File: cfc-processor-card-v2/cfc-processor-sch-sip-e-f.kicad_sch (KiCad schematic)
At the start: 5 parts, among them U7 OSD3358-1G-ISM

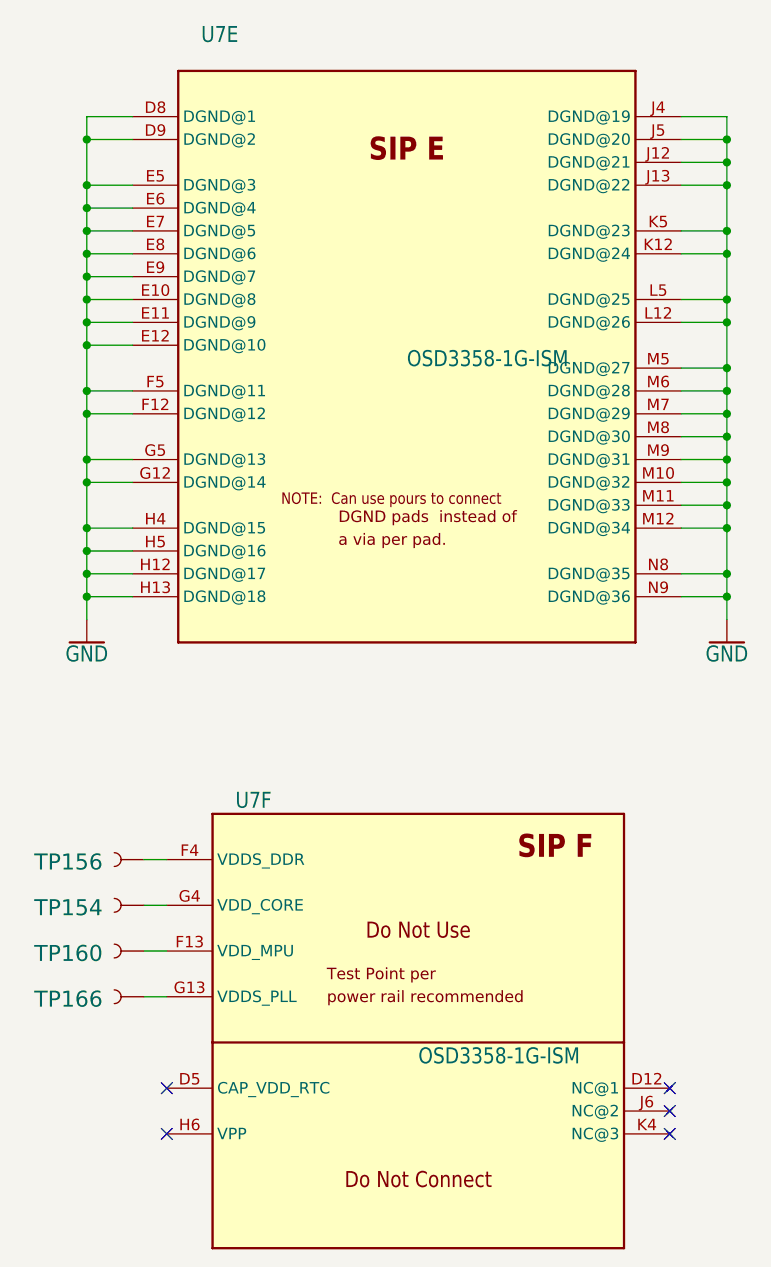
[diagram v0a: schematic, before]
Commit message: CFC processor schematic Change
changed to hierarchy view, changed all global net labels to hierarchy labels, changed all resistor, capacitor, and ground symbols to modern oresat labels. Deleted connectors sheet and added .history to gitignore.
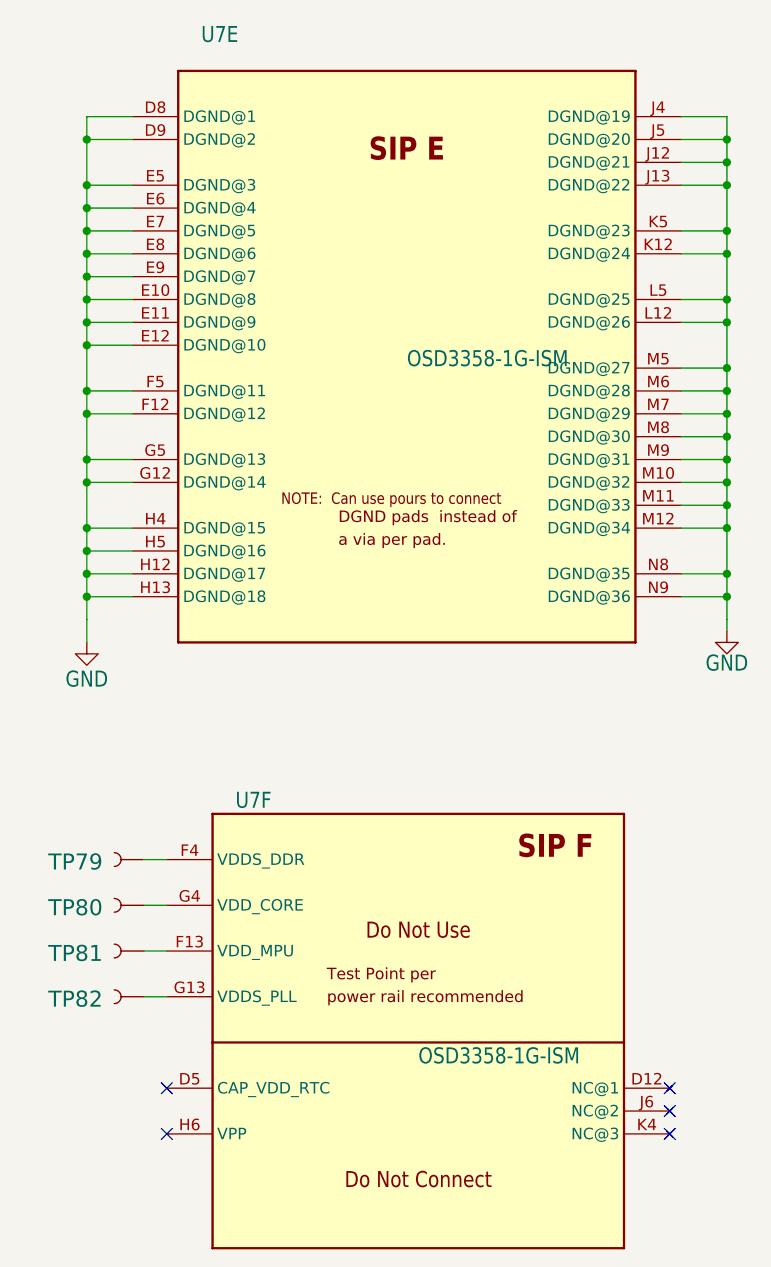
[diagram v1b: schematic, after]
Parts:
- renumbered TP156 to TP79, TP154 to TP80, TP160 to TP81, TP166 to TP82

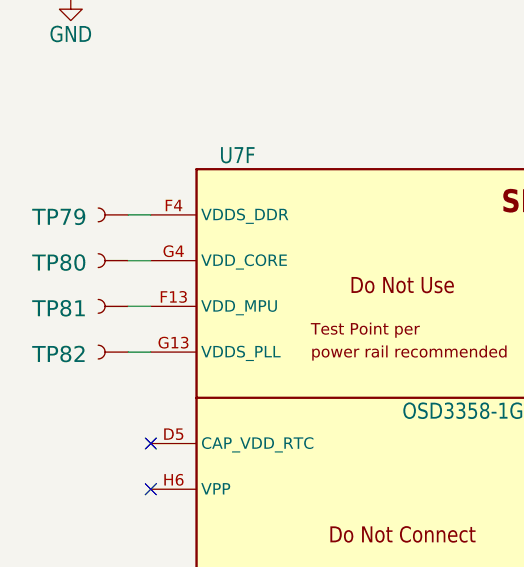
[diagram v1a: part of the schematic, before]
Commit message: Updated OPD
couple of resistors and caps added to schematic. Changed USB ESD clamp VDD to 3.3v instead of octavo created VDD line.
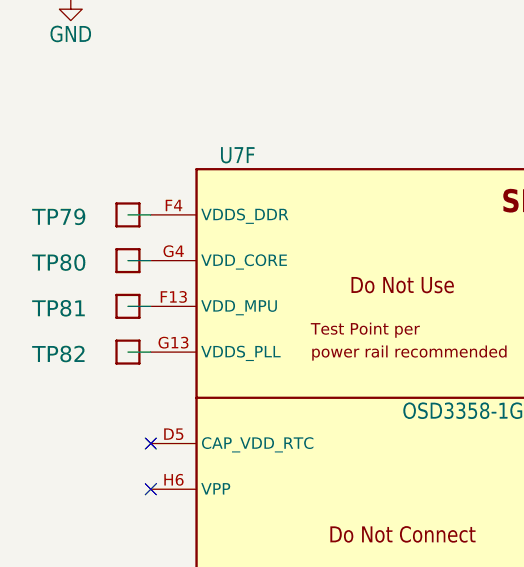
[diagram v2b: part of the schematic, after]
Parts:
- TP79, TP80, TP81, TP82: footprint cfc-card:PAD.03X.04 -> oresat-misc:TestPoint_Pad_D1.0mm; symbol cfc-card-eagle-import:TEST-POINT3X4 -> Oresat Misc:Test-Point-1mm-round
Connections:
- net at U7.G4 (VDD_CORE): now also TP80.1; no longer TP80.P$1 (1)
- net at U7.F13 (VDD_MPU): now also TP81.1; no longer TP81.P$1 (1)
- net at U7.F4 (VDDS_DDR): now also TP79.1; no longer TP79.P$1 (1)
- net at U7.G13 (VDDS_PLL): now also TP82.1; no longer TP82.P$1 (1)
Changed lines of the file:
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@@
 	)
 	(symbol
-		(lib_id "cfc-card-eagle-import:TEST-POINT3X4")
+		(lib_id "Oresat Misc:Test-Point-1mm-round")
 		(at 185.42 152.4 180)
 		(unit 1)
@@
 			)
 		)
-		(property "Footprint" "cfc-card:PAD.03X.04"
-			(at 185.42 152.4 0)
+		(property "Footprint" "oresat-misc:TestPoint_Pad_D1.0mm"
+			(at 185.42 162.56 0)
 			(hide yes)
 			(show_name no)
@@
 			)
 		)
-		(property "Description" "SparkFun Test Points\n\nBare copper test points for troubleshooting or In-Circuit-Testing. These are used by our Production team for verifying production board runs using pogo-pins on test beds.\n\nSparkFun Products:\n\n• SparkFun LSM9DS1 Breakout\n• SparkFun PSOC\n• https://www.sparkfun.com/products/13879 SparkFun Load Cell Amplifier"
+		(property "Description" "1mm round SMT test point"
 			(at 185.42 152.4 0)
 			(hide yes)
@@
 			)
 		)
-		(pin "P$1"
+		(pin "1"
 		)
 		(instances
@@
 	)
 	(symbol
-		(lib_id "cfc-card-eagle-import:TEST-POINT3X4")
+		(lib_id "Oresat Misc:Test-Point-1mm-round")
 		(at 185.42 162.56 180)
 		(unit 1)
@@
 			)
 		)
-		(property "Footprint" "cfc-card:PAD.03X.04"
-			(at 185.42 162.56 0)
+		(property "Footprint" "oresat-misc:TestPoint_Pad_D1.0mm"
+			(at 185.42 172.72 0)
 			(hide yes)
 			(show_name no)
@@
 			)
 		)
-		(property "Description" "SparkFun Test Points\n\nBare copper test points for troubleshooting or In-Circuit-Testing. These are used by our Production team for verifying production board runs using pogo-pins on test beds.\n\nSparkFun Products:\n\n• SparkFun LSM9DS1 Breakout\n• SparkFun PSOC\n• https://www.sparkfun.com/products/13879 SparkFun Load Cell Amplifier"
+		(property "Description" "1mm round SMT test point"
 			(at 185.42 162.56 0)
 			(hide yes)
@@
 			)
 		)
-		(pin "P$1"
+		(pin "1"
 		)
 		(instances
@@
 	)
 	(symbol
-		(lib_id "cfc-card-eagle-import:TEST-POINT3X4")
+		(lib_id "Oresat Misc:Test-Point-1mm-round")
 		(at 185.42 157.48 180)
 		(unit 1)
@@
 			)
 		)
-		(property "Footprint" "cfc-card:PAD.03X.04"
-			(at 185.42 157.48 0)
+		(property "Footprint" "oresat-misc:TestPoint_Pad_D1.0mm"
+			(at 185.42 167.64 0)
 			(hide yes)
 			(show_name no)
@@
 			)
 		)
-		(property "Description" "SparkFun Test Points\n\nBare copper test points for troubleshooting or In-Circuit-Testing. These are used by our Production team for verifying production board runs using pogo-pins on test beds.\n\nSparkFun Products:\n\n• SparkFun LSM9DS1 Breakout\n• SparkFun PSOC\n• https://www.sparkfun.com/products/13879 SparkFun Load Cell Amplifier"
+		(property "Description" "1mm round SMT test point"
 			(at 185.42 157.48 0)
 			(hide yes)
@@
 			)
 		)
-		(pin "P$1"
+		(pin "1"
 		)
 		(instances
@@
 	)
 	(symbol
-		(lib_id "cfc-card-eagle-import:TEST-POINT3X4")
+		(lib_id "Oresat Misc:Test-Point-1mm-round")
 		(at 185.42 147.32 180)
 		(unit 1)
@@
 			)
 		)
-		(property "Footprint" "cfc-card:PAD.03X.04"
-			(at 185.42 147.32 0)
+		(property "Footprint" "oresat-misc:TestPoint_Pad_D1.0mm"
+			(at 185.42 157.48 0)
 			(hide yes)
 			(show_name no)
@@
 			)
 		)
-		(property "Description" "SparkFun Test Points\n\nBare copper test points for troubleshooting or In-Circuit-Testing. These are used by our Production team for verifying production board runs using pogo-pins on test beds.\n\nSparkFun Products:\n\n• SparkFun LSM9DS1 Breakout\n• SparkFun PSOC\n• https://www.sparkfun.com/products/13879 SparkFun Load Cell Amplifier"
+		(property "Description" "1mm round SMT test point"
 			(at 185.42 147.32 0)
 			(hide yes)
@@
 			)
 		)
-		(pin "P$1"
+		(pin "1"
 		)
 		(instances

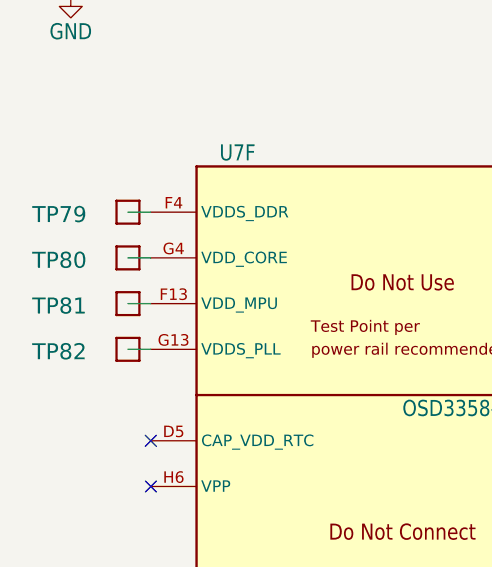
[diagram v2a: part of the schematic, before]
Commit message: Update
Added pull down resistors and removed therm + and sensor enable and added i2c support for cfc sensor card.
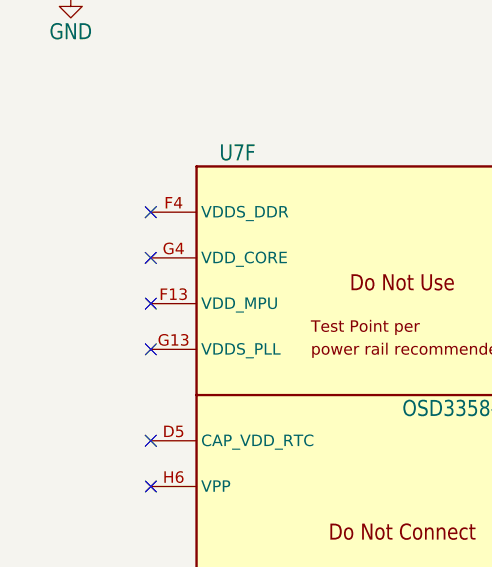
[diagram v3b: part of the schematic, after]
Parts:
- removed TP79, TP80, TP81, TP82: TEST-POINT3X4, oresat-misc:TestPoint_Pad_D1.0mm, symbol Oresat Misc:Test-Point-1mm-round
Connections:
- no-connect marks 5 -> 9
